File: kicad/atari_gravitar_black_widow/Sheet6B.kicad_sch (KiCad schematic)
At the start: 20 parts

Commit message: REVIEWS AND FINALS
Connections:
- net +5V: now also A_7.14 (VCC)
- net GND: now also A_7.7 (GND), N_4.8 (GND)
- net at M_4.9: now also K_3.9 (2Q), K_5.3
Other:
- note added: "Address Controller"
- note added: "Decoder Disable"
- note added: "Signature Analysis Flag"
- note added: "State Machine"
- note added: "State Machine Clock"
- note added: "State Machine Clock Logic"
- note removed: "ADDRESS CONTROLLER"
- note removed: "DECODER DISABLE"
- note removed: "SIGNATURE ANALYSIS FLAG"
- note removed: "STATE MACHINE"
- note removed: "STATE MACHINE CLOCK"
- note removed: "STATE MACHINE CLOCK LOGIC"
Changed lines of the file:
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@@
   (junction (at 141.605 198.755) (diameter 0) (color 0 0 0 0)
-  )
-  (junction (at 134.62 175.26) (diameter 0) (color 0 0 0 0)
   )
   (junction (at 390.525 82.55) (diameter 0) (color 0 0 0 0)
@@
     (stroke (width 0) (type default) (color 0 0 0 0))
   )
-  (wire (pts (xy 134.62 175.26) (xy 74.93 175.26))
+  (wire (pts (xy 67.31 175.26) (xy 74.93 175.26))
     (stroke (width 0) (type default) (color 0 0 0 0))
   )
@@
     (stroke (width 0) (type default) (color 0 0 0 0))
   )
-  (wire (pts (xy 342.9 300.355) (xy 342.9 308.61))
-    (stroke (width 0) (type default) (color 0 0 0 0))
-  )
   (wire (pts (xy 67.31 116.205) (xy 424.18 116.205))
     (stroke (width 0) (type default) (color 0 0 0 0))
@@
     (stroke (width 0) (type default) (color 0 0 0 0))
   )
-  (wire (pts (xy 135.89 175.26) (xy 134.62 175.26))
-    (stroke (width 0) (type default) (color 0 0 0 0))
-  )
   (wire (pts (xy 417.83 128.905) (xy 417.83 170.18))
     (stroke (width 0) (type default) (color 0 0 0 0))
@@
     (stroke (width 0) (type default) (color 0 0 0 0))
   )
+  (wire (pts (xy 74.93 175.26) (xy 134.62 175.26))
+    (stroke (width 0) (type default) (color 0 0 0 0))
+  )
   (wire (pts (xy 367.665 86.995) (xy 367.665 95.25))
     (stroke (width 0) (type default) (color 0 0 0 0))
@@
     (stroke (width 0) (type default) (color 0 0 0 0))
   )
-  (wire (pts (xy 74.93 175.26) (xy 67.31 175.26))
+  (wire (pts (xy 342.9 299.72) (xy 342.9 308.61))
     (stroke (width 0) (type default) (color 0 0 0 0))
   )
@@
     (stroke (width 0) (type default) (color 0 0 0 0))
   )
-  (wire (pts (xy 135.89 171.45) (xy 133.35 171.45))
+  (wire (pts (xy 133.35 171.45) (xy 137.16 171.45))
     (stroke (width 0) (type default) (color 0 0 0 0))
   )
@@
     (effects (font (size 1.27 1.27)) (justify left bottom))
   )
-  (text "SIGNATURE ANALYSIS FLAG" (at 342.265 73.025 0)
+  (text "Signature Analysis Flag" (at 315.722 76.2 0)
     (effects (font (size 2.54 2.54) (thickness 0.508) bold) (justify left bottom))
   )
@@
     (effects (font (size 1.27 1.27)) (justify left bottom))
   )
-  (text "STATE MACHINE CLOCK LOGIC" (at 83.82 245.11 0)
+  (text "State Machine Clock Logic" (at 83.82 245.11 0)
     (effects (font (size 2.54 2.54) (thickness 0.508) bold) (justify left bottom))
   )
@@
     (effects (font (size 1.27 1.27)) (justify left bottom))
   )
-  (text "DECODER DISABLE" (at 321.945 170.18 0)
+  (text "Decoder Disable" (at 321.945 170.18 0)
     (effects (font (size 2.54 2.54) (thickness 0.508) bold) (justify left bottom))
   )
@@
     (effects (font (size 1.27 1.27)) (justify left bottom))
   )
-  (text "ADDRESS CONTROLLER" (at 431.8 73.025 0)
+  (text "Address Controller" (at 412.115 76.073 0)
     (effects (font (size 2.54 2.54) (thickness 0.508) bold) (justify left bottom))
   )
@@
     (effects (font (size 1.27 1.27)) (justify left bottom))
   )
-  (text "STATE MACHINE\nCLOCK" (at 269.24 172.72 0)
+  (text "State Machine Clock\n" (at 269.24 172.72 0)
     (effects (font (size 2.54 2.54) (thickness 0.508) bold) (justify left bottom))
   )
@@
     (effects (font (size 1.27 1.27)) (justify left bottom))
   )
-  (text "STATE MACHINE" (at 233.045 259.715 0)
+  (text "State Machine" (at 233.045 259.715 0)
     (effects (font (size 2.54 2.54) (thickness 0.508) bold) (justify left bottom))
   )
@@
     (in_bom yes) (on_board yes)
     (property "Reference" "M_4" (id 0) (at 151.13 170.18 0))
-    (property "Value" "LS27" (id 1) (at 151.13 172.72 0))
+    (property "Value" "LS27" (id 1) (at 151.003 174.498 0))
     (property "Footprint" "" (id 2) (at 151.13 171.45 0)
       (effects (font (size 1.27 1.27)) hide)
@@
       (effects (font (size 1.27 1.27)) hide)
     )
+    (pin "1")
+  )
+  (symbol (lib_id "power:GND") (at 292.1 224.155 0) (unit 1)
+    (in_bom yes) (on_board yes)
+    (property "Reference" "#PWR0279" (id 0) (at 292.1 230.505 0)
+      (effects (font (size 1.27 1.27)) hide)
+    )
+    (property "Value" "GND" (id 1) (at 292.227 228.5492 0))
+    (property "Footprint" "" (id 2) (at 292.1 224.155 0)
+      (effects (font (size 1.27 1.27)) hide)
+    )
+    (property "Datasheet" "" (id 3) (at 292.1 224.155 0)
+      (effects (font (size 1.27 1.27)) hide)
+    )
+    (pin "1")
+  )
+  (symbol (lib_id "power:+5V") (at 292.1 203.835 0) (unit 1)
+    (in_bom yes) (on_board yes)
+    (property "Reference" "#PWR0280" (id 0) (at 292.1 207.645 0)
+      (effects (font (size 1.27 1.27)) hide)
+    )
+    (property "Value" "+5V" (id 1) (at 292.481 199.4408 0))
+    (property "Footprint" "" (id 2) (at 292.1 203.835 0)
+      (effects (font (size 1.27 1.27)) hide)
+    )
+    (property "Datasheet" "" (id 3) (at 292.1 203.835 0)
+      (effects (font (size 1.27 1.27)) hide)
+    )

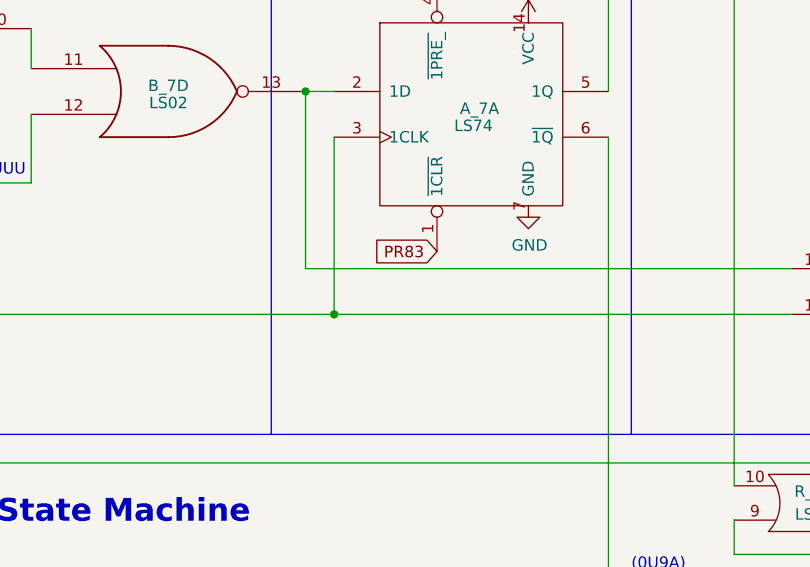
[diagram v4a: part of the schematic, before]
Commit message: 20 warnings left kicad 6.0
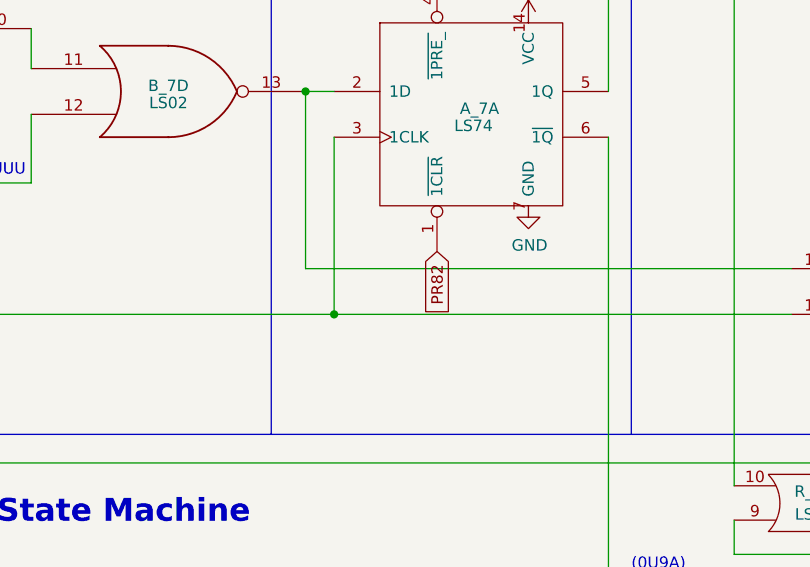
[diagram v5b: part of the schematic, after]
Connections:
- net PR83 is gone; now on net PR82: A_7.1 (~{1CLR})
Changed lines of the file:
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@@
-    )
-  )
-  (global_label "PR83" (shape input) (at 281.94 229.235 180) (fields_autoplaced)
-    (effects (font (size 1.27 1.27)) (justify right))
-    (property "Intersheet References" "${INTERSHEET_REFS}" (id 0) (at 0 0 0)
-      (effects (font (size 1.27 1.27)) hide)
     )
   )
@@
       (effects (font (size 1.27 1.27)) hide)
     )
+  )
+  (global_label "PR82" (shape input) (at 281.94 229.235 270) (fields_autoplaced)
+    (effects (font (size 1.27 1.27)) (justify right))
+    (property "Intersheet References" "${INTERSHEET_REFS}" (id 0) (at 372.745 422.91 0)
+      (effects (font (size 1.27 1.27)) hide)
+    )

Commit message: place ttl
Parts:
- A_7, B_7: footprint (none) -> Star_Wars_Vector_PCB:DIP14
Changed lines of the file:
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@@
     (property "Reference" "B_7" (id 0) (at 221.615 203.2 0))
     (property "Value" "LS02" (id 1) (at 221.615 206.375 0))
-    (property "Footprint" "" (id 2) (at 221.615 204.47 0)
+    (property "Footprint" "Star_Wars_Vector_PCB:DIP14" (id 2) (at 221.615 204.47 0)
       (effects (font (size 1.27 1.27)) hide)
     )
@@
     (property "Reference" "B_7" (id 0) (at 252.095 210.82 0))
     (property "Value" "LS02" (id 1) (at 252.095 212.725 0))
-    (property "Footprint" "" (id 2) (at 252.095 211.455 0)
+    (property "Footprint" "Star_Wars_Vector_PCB:DIP14" (id 2) (at 252.095 211.455 0)
       (effects (font (size 1.27 1.27)) hide)
     )
@@
       (effects (font (size 1.27 1.27)) (justify left))
     )
-    (property "Footprint" "" (id 2) (at 286.385 220.345 0)
+    (property "Footprint" "Star_Wars_Vector_PCB:DIP14" (id 2) (at 286.385 220.345 0)
       (effects (font (size 7.62 7.62)) hide)
     )
@@
     (property "Reference" "A_7" (id 0) (at 336.55 232.41 0))
     (property "Value" "LS74" (id 1) (at 336.55 234.95 0))
-    (property "Footprint" "" (id 2) (at 337.185 240.03 0)
+    (property "Footprint" "Star_Wars_Vector_PCB:DIP14" (id 2) (at 337.185 240.03 0)
       (effects (font (size 7.62 7.62)) hide)
     )

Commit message: more ttl placements
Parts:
- H_7: footprint (none) -> Star_Wars_Vector_PCB:DIP16
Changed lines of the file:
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@@
     (property "Reference" "H_7" (id 0) (at 382.27 238.76 0))
     (property "Value" "LS42" (id 1) (at 382.27 241.3 0))
-    (property "Footprint" "" (id 2) (at 382.27 240.03 0)
+    (property "Footprint" "Star_Wars_Vector_PCB:DIP16" (id 2) (at 382.27 240.03 0)
       (effects (font (size 1.27 1.27)) hide)
     )

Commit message: more chip layouts
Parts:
- J_3, J_5, K_3, K_5, K_6: footprint (none) -> Star_Wars_Vector_PCB:DIP14
- J_9: footprint (none) -> Star_Wars_Vector_PCB:DDIP40
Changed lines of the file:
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@@
     (property "Reference" "J_3" (id 0) (at 382.27 92.71 0))
     (property "Value" "LS04" (id 1) (at 378.46 95.25 0))
-    (property "Footprint" "" (id 2) (at 379.095 95.25 0)
+    (property "Footprint" "Star_Wars_Vector_PCB:DIP14" (id 2) (at 379.095 95.25 0)
       (effects (font (size 1.27 1.27)) hide)
     )
@@
       (effects (font (size 1.524 1.524)))
     )
-    (property "Footprint" "" (id 2) (at 447.04 158.115 0)
+    (property "Footprint" "Star_Wars_Vector_PCB:DDIP40" (id 2) (at 447.04 158.115 0)
       (effects (font (size 1.524 1.524)) hide)
     )
@@
     (property "Reference" "K_6" (id 0) (at 91.44 197.485 0))
     (property "Value" "LS02" (id 1) (at 91.44 200.025 0))
-    (property "Footprint" "" (id 2) (at 91.44 198.755 0)
+    (property "Footprint" "Star_Wars_Vector_PCB:DIP14" (id 2) (at 91.44 198.755 0)
       (effects (font (size 1.27 1.27)) hide)
     )
@@
     (property "Reference" "K_5" (id 0) (at 181.61 172.72 0))
     (property "Value" "LS02" (id 1) (at 181.61 175.26 0))
-    (property "Footprint" "" (id 2) (at 181.61 173.99 0)
+    (property "Footprint" "Star_Wars_Vector_PCB:DIP14" (id 2) (at 181.61 173.99 0)
       (effects (font (size 1.27 1.27)) hide)
     )
@@
       (effects (font (size 1.27 1.27)) (justify left))
     )
-    (property "Footprint" "" (id 2) (at 180.975 196.215 0)
+    (property "Footprint" "Star_Wars_Vector_PCB:DIP14" (id 2) (at 180.975 196.215 0)
       (effects (font (size 1.27 1.27)) hide)
     )
@@
     (property "Reference" "K_3" (id 0) (at 121.92 200.025 0))
     (property "Value" "LS74" (id 1) (at 121.92 202.565 0))
-    (property "Footprint" "" (id 2) (at 122.555 207.645 0)
+    (property "Footprint" "Star_Wars_Vector_PCB:DIP14" (id 2) (at 122.555 207.645 0)
       (effects (font (size 7.62 7.62)) hide)
     )
@@
       (effects (font (size 1.27 1.27)) (justify left))
     )
-    (property "Footprint" "" (id 2) (at 219.075 221.615 0)
-      (effects (font (size 1.27 1.27)) hide)
-    )
+    (property "Footprint" "Star_Wars_Vector_PCB:DIP14" (id 2) (at 219.075 221.615 0)
+      (effects (font (size 1.27 1.27)) hide)
+    )
